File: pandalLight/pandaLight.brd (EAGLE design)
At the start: 100 x 50 mm, 159 parts, among them J1 PJ-037A, U1 MIC23450AAAYML, U12 N25Q128AF8, U13 TPD12S016PWR, U14 AS4C128M16D3, U15 PMOD-2X6, U16 PMOD-2X6, U17 PLR135-T10, U18 PLT133-T10W, U19 PLR135-T10, U2 6SLX45CSG324, U20 TP10SQ, U21 TP10SQ, U22 PAN1322, U23 6SLX9TQG144, U3 TPD4S014SON, U4 FT2232HL, U5 93LC46BT-I/OT, U6 51, U7 51, U8 TPD12S016PWR, X1 USBUB-S, X2 HDMI_RECEPTICAL_A, X4 HDMI_RECEPTICAL_A, Y1 403, Y2 20Mhz

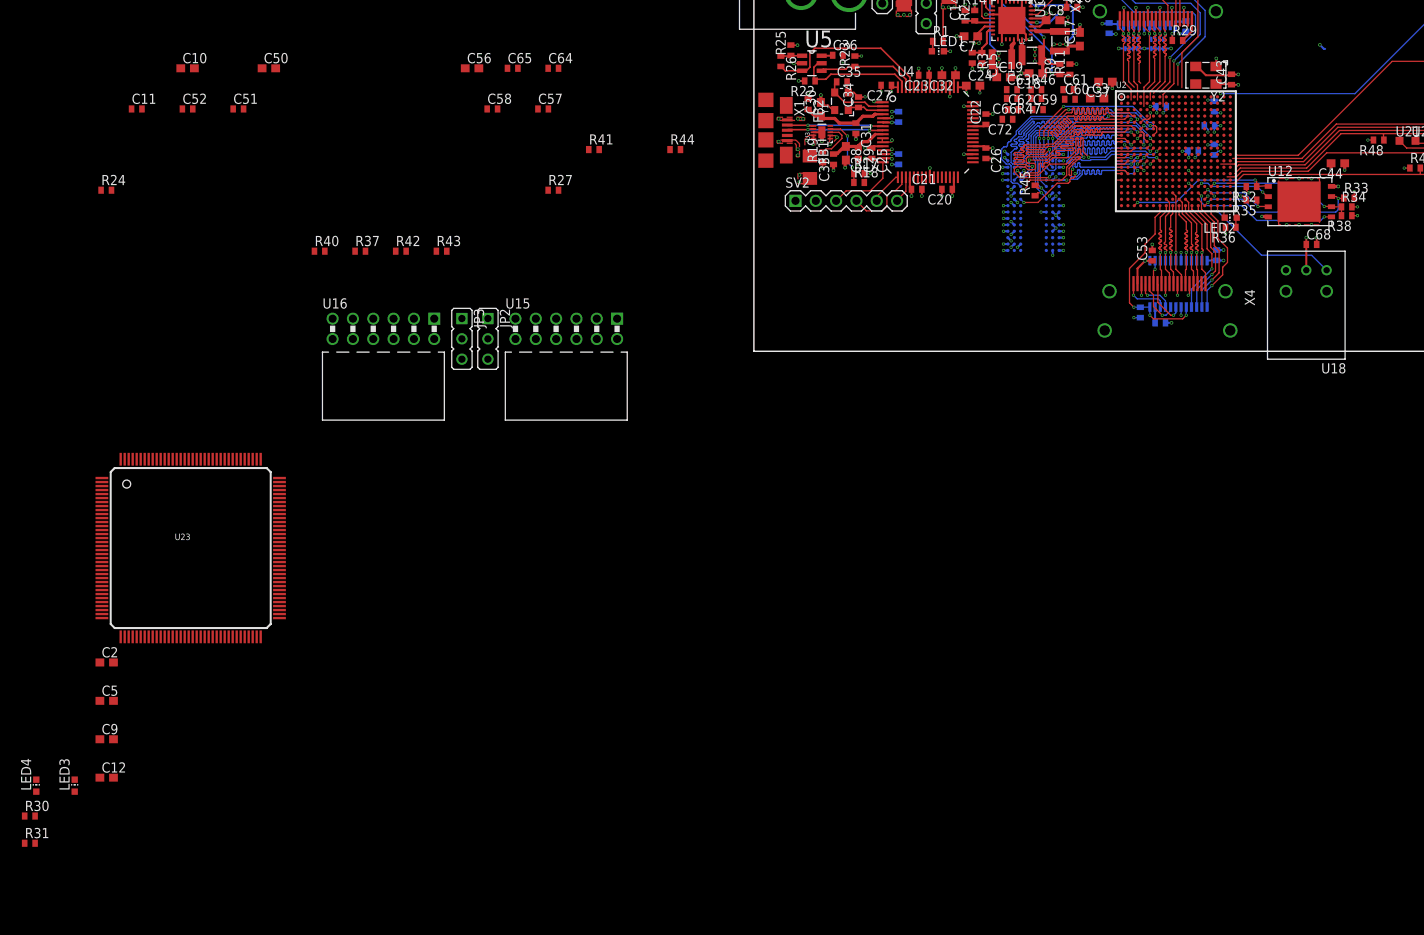
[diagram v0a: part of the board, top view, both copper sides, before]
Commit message: Continued switching to LX9
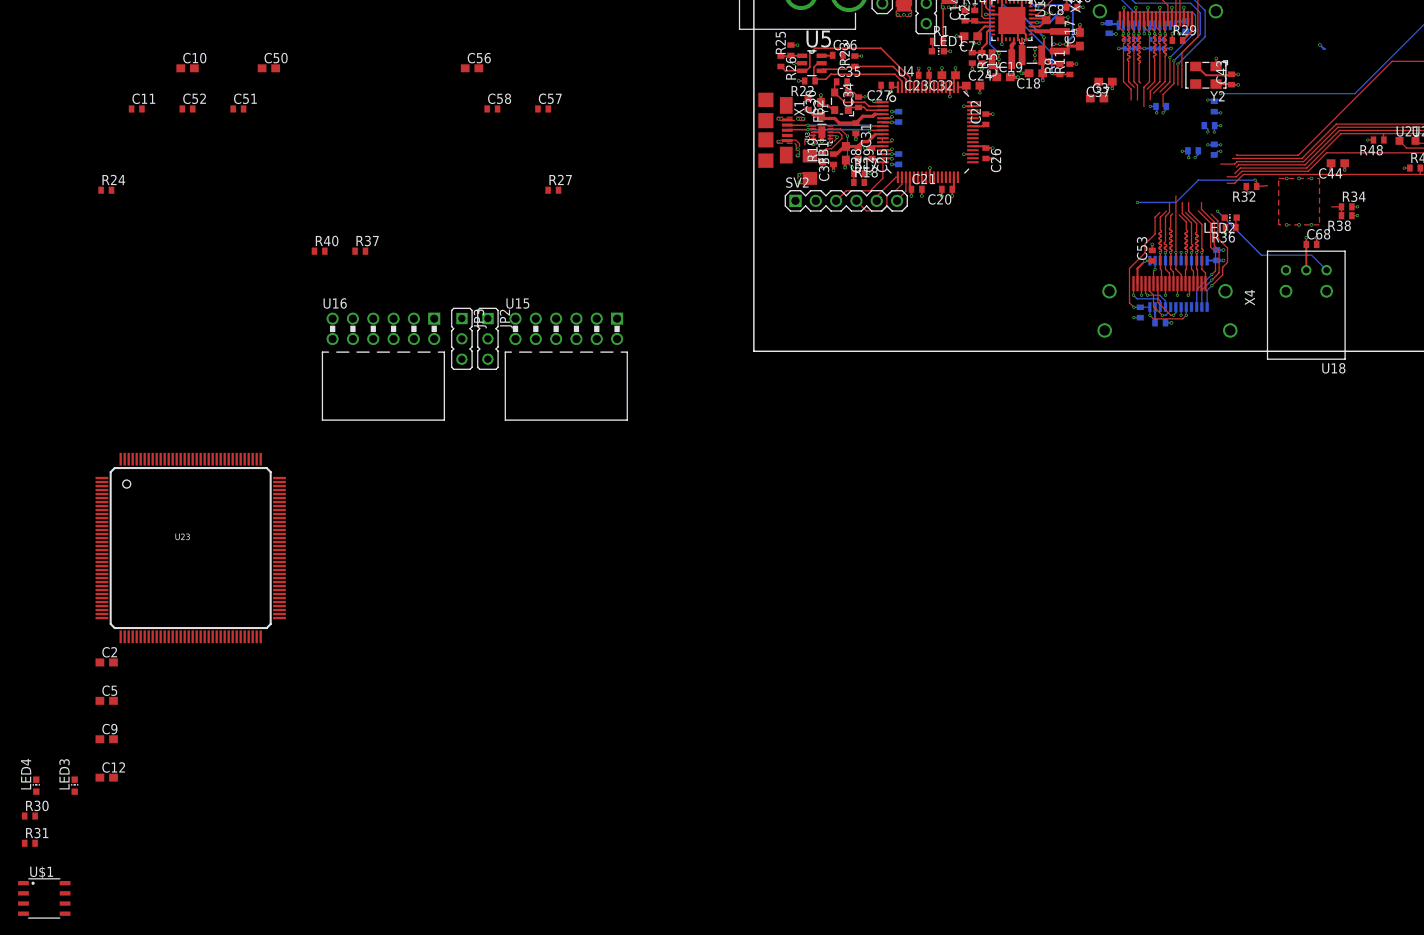
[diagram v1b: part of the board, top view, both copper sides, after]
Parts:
- removed C59, C60: 1u, pandaLight:0402
- removed C61, C62, C63, C64, C65, C66, C72: 0.1u, pandaLight:0402
- removed R33, R35: 10k, pandaLight:0402
- removed R41: 120, pandaLight:0402
- removed R42, R43: 4.7k, pandaLight:0402
- removed R44: 240, pandaLight:0402
- removed R45: 100, pandaLight:0402
- removed R46, R47: 1k, pandaLight:0402
- removed U12: N25Q128AF8, pandaLight:V-PDFN-8_8X6
- removed U14: AS4C128M16D3, pandaLight:96-FBGA_13X9
- removed U2: 6SLX45CSG324, pandaLight:CS324
- added U$1: M25P40-VMN, pandaLight:SO8N
- R30, R31: value 220 -> 1k
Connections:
- removed net +1V5_VREF: C63.2, C64.1, C65.1, C66.1, C72.1, R46.1, R47.2, U14.H1, U14.M8, U2.C1, U2.M5, U2.N3
- removed net DDR3_A0: U14.N3, U2.J7
- removed net DDR3_A1: U14.P7, U2.J6
- removed net DDR3_A10: U14.L7, U2.F4
- removed net DDR3_A11: U14.R7, U2.D3
- removed net DDR3_A12: U14.N7, U2.G6
- removed net DDR3_A2: U14.P3, U2.H5
- removed net DDR3_A3: U14.N2, U2.L7
- removed net DDR3_A4: U14.P8, U2.F3
- removed net DDR3_A5: U14.P2, U2.H4
- removed net DDR3_A6: U14.R8, U2.H3
- removed net DDR3_A7: U14.R2, U2.H6
- removed net DDR3_A8: U14.T8, U2.D2
- removed net DDR3_A9: U14.R3, U2.D1
- removed net DDR3_BA0: U14.M2, U2.F2
- removed net DDR3_BA1: U14.N8, U2.F1
- removed net DDR3_BA2: U14.M3, U2.E1
- removed net DDR3_CAS#: U14.K3, U2.K5
- removed net DDR3_CK: R45.1, U14.J7, U2.G3
- removed net DDR3_CK#: R45.2, U14.K7, U2.G1
- removed net DDR3_CKE: R42.2, U14.K9, U2.H7
- removed net DDR3_DQ0: U14.E3, U2.L2
- removed net DDR3_DQ1: U14.F7, U2.L1
- removed net DDR3_DQ10: U14.C8, U2.N2
- removed net DDR3_DQ11: U14.C2, U2.N1
- removed net DDR3_DQ12: U14.A7, U2.T2
- removed net DDR3_DQ13: U14.A2, U2.T1
- removed net DDR3_DQ14: U14.B8, U2.U2
- removed net DDR3_DQ15: U14.A3, U2.U1
- removed net DDR3_DQ2: U14.F2, U2.K2
- removed net DDR3_DQ3: U14.F8, U2.K1
- removed net DDR3_DQ4: U14.H3, U2.H2
- removed net DDR3_DQ5: U14.H8, U2.H1
- removed net DDR3_DQ6: U14.G2, U2.J3
- removed net DDR3_DQ7: U14.H7, U2.J1
- removed net DDR3_DQ8: U14.D7, U2.M3
- removed net DDR3_DQ9: U14.C3, U2.M1
- removed net DDR3_LDM: U14.E7, U2.K3
- removed net DDR3_LDQS: U14.F3, U2.L4
- removed net DDR3_LDQS#: U14.G3, U2.L3
- removed net DDR3_ODT: U14.K1, U2.K6
- removed net DDR3_RAS#: U14.J3, U2.L5
- removed net DDR3_RESET#: R43.2, U14.T2, U2.E4
- removed net DDR3_UDM: U14.D3, U2.K4
- removed net DDR3_UDQS: U14.C7, U2.P2
- removed net DDR3_UDQS#: U14.B7, U2.P1
- removed net DDR3_WE#: U14.L3, U2.E3
- removed net HDMI_TX0_HPD_3V3: U13.4, U2.V12
- removed net M3_RZQ: R41.1, U2.L6
- removed net N$46: R33.1, U12.7, U2.V14
- removed net N$53: LED4.C, R31.2
- net +1V5: no longer C59.1, C60.1, C61.1, C62.1, C63.1, R46.2, U14.A1, U14.A8, U14.B2, U14.C1, U14.C9, U14.D2, U14.D9, U14.E9, U14.F1, U14.G7, U14.H2, U14.H9, U14.K2, U14.K8, U14.N1, U14.N9, U14.R1, U14.R9, U2.E2, U2.G4, U2.J2, U2.J5, U2.M4, U2.R2
- net +3V3: now also R30.2, R31.2, U$1.3, U$1.7, U$1.8, U23.P103, U23.P122, U23.P125, U23.P135, U23.P42, U23.P63, U23.P69, U23.P76, U23.P86; no longer LED3.A, LED4.A, R33.2, R35.2, U12.8, U2.P9, U2.R12, U2.R6, U2.T15, U2.U14, U2.U4, U2.U9
- net GND: now also U$1.4, U23.P60; no longer C59.2, C60.2, C61.2, C62.2, C64.2, C65.2, C66.2, C72.2, R41.2, R42.1, R43.1, R44.1, R47.1, U12.4, U12.ETP, U14.A9, U14.B1, U14.B3, U14.B9, U14.D1, U14.D8, U14.E1, U14.E2, U14.E8, U14.F9, U14.G1, U14.G8, U14.G9, U14.J2, U14.J8, U14.L2, U14.M1, U14.M9, U14.P1, U14.P9, U14.T1, U14.T9, U2.A1, U2.A18, U2.B13, U2.B7, U2.C16, U2.C3, U2.D10, U2.D5, U2.E15, U2.G12, U2.G17, U2.G2, U2.G5, U2.H10, U2.H8, U2.J11, U2.J15, U2.J4, U2.J9, U2.K10, U2.K8, U2.L11, U2.L9, U2.M17, U2.M2, U2.M6, U2.N12, U2.N13, U2.R1, U2.R14, U2.R18, U2.R4, U2.R9, U2.T16, U2.U12, U2.U6, U2.V1, U2.V18
- net HDMI_TX0_CEC_3V3: no longer U2.V15
- net HDMI_TX0_CLK_N: now also U23.P50; no longer U2.V8
- net HDMI_TX0_CLK_P: now also U23.P51; no longer U2.U8
- net HDMI_TX0_CTRL_EN: no longer U2.V7
- net HDMI_TX0_DATA0_N: now also U23.P55; no longer U2.V9
- net HDMI_TX0_DATA0_P: now also U23.P56; no longer U2.T9
- net HDMI_TX0_DATA1_N: now also U23.P57; no longer U2.V10
- net HDMI_TX0_DATA1_P: now also U23.P58; no longer U2.U10
- net HDMI_TX0_DATA2_N: now also U23.P61; no longer U2.V11
- net HDMI_TX0_DATA2_P: no longer U13.23, U2.U11
- net HDMI_TX0_SCL_3V3: no longer U2.U13
- net HDMI_TX0_SDA_3V3: no longer U2.V13
- net N$3: now also LED4.A, R31.1; no longer R44.2, U14.L8
- net N$33: now also U23.P71; no longer U2.V17
- net N$34: now also U23.P37; no longer U2.V2
- net N$35: now also U23.P144
- net N$37: now also LED3.A, R30.1; no longer LED3.C, R30.2
- net N$39: now also U23.P39; no longer U2.U3
- net N$40: now also U$1.5, U23.P64; no longer U12.5, U2.T13
- net N$41: now also U$1.1, U23.P38; no longer U12.1, U2.V3
- net N$42: now also U$1.6, U23.P70; no longer U12.6, U2.R15
- net N$43: now also U$1.2, U23.P65; no longer U12.2, U2.R13
- net N$44: now also U13.23, U23.P62; no longer R35.1, U12.3, U2.T14
- net TOS_OUT0: no longer U2.V16
- net USB_CTS#: now also U23.P111
- net USB_DCD#: now also U23.P118
- net USB_DSR#: now also U23.P117
- net USB_DTR#: now also U23.P116
- net USB_RI#: now also U23.P119
- net USB_RTS#: now also U23.P112
- net USB_RXD: now also U23.P114
- net USB_RXLED#: now also LED3.C; no longer R30.1
- net USB_TXD: now also U23.P115
- net USB_TXLED#: now also LED4.C; no longer R31.1
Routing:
- net DDR3_WE#: track 26.5 -> 0.00 mm, vias 1 -> 0
- net DDR3_A4: track 26.5 -> 0.00 mm, vias 1 -> 0
- net DDR3_A5: track 26.5 -> 0.00 mm, vias 1 -> 0
- net DDR3_BA1: track 26.5 -> 0.00 mm, vias 1 -> 0
- net DDR3_A11: track 26.5 -> 0.00 mm, vias 1 -> 0
- net DDR3_A2: track 26.5 -> 0.00 mm, vias 1 -> 0
- net DDR3_A0: track 26.5 -> 0.00 mm, vias 3 -> 0
- net DDR3_RAS#: track 26.5 -> 0.00 mm, vias 3 -> 0
- net DDR3_BA0: track 26.5 -> 0.00 mm, vias 1 -> 0
- net DDR3_A1: track 26.5 -> 0.00 mm, vias 1 -> 0
- net DDR3_A9: track 26.5 -> 0.00 mm, vias 1 -> 0
- net DDR3_A7: track 26.5 -> 0.00 mm, vias 1 -> 0
- net DDR3_CAS#: track 26.5 -> 0.00 mm, vias 3 -> 0
- net DDR3_A3: track 26.5 -> 0.00 mm, vias 3 -> 0
- net DDR3_A6: track 26.5 -> 0.00 mm, vias 1 -> 0
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
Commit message: Made new signal connections; Removed old signals; New buck regulator; Reset the board layout
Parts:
- removed C15, C16, C69: 0.1u, pandaLight:0402
- removed C17, C18, C19: 4.7u, pandaLight:0603
- removed L2: 1u, 3A, pandaLight:1008
- removed L5: 47u, pandaLight:0603
- removed R10, R12, R14, R7: 100k, pandaLight:0402
- removed R11: 221k, pandaLight:0402
- removed R13: 274k, pandaLight:0402
- removed R15: 294k, pandaLight:0402
- removed R2, R3, R4: 51, pandaLight:0402
- removed R6: 71.5k, pandaLight:0402
- removed R9: 316k, pandaLight:0402
- removed U1: MIC23450AAAYML, pandaLight:QFN-32-5X5
- removed U19: PLR135-T10, pandaLight:PLR135-T10_PLT133-T10W
- added C13: 10u, pandaLight:0603
- added SV3: (no value), pandaLight:MA02-1
- added U$2: MIC2230-XXYML, pandaLight:MLF-12
- C14: value 0.1u -> 10u; device pandaLight:0402 -> pandaLight:0603
- L1, L3: value 1u, 3A -> 2.2u, 1.3A
- R5: value 309k -> 100k
- moved U20 208.2 mm to (-102.9, 120.7)
- moved C68 198.7 mm to (-102.9, 111.8)
- moved C67 197.0 mm to (-97.8, 111.8), turned to 0 degrees
- moved R49 192.6 mm to (-82.5, 121.9)
- moved L4 190.1 mm to (-87.6, 121.9), turned to 0 degrees
- moved R31 187.4 mm to (-52.1, 121.9)
- moved R30 185.2 mm to (-47.0, 121.9)
- moved R48 182.6 mm to (-77.5, 121.9), turned to 0 degrees
- moved C44 180.9 mm to (-87.6, 106.7), turned to 0 degrees
- moved C55 180.6 mm to (-92.7, 111.8), flipped to the top, turned to 0 degrees
- moved R38 176.1 mm to (-67.3, 121.9), turned to 0 degrees
- moved C54 175.7 mm to (-87.6, 111.8), flipped to the top, turned to 0 degrees
- moved R39 168.1 mm to (-72.4, 121.9), flipped to the top, turned to 0 degrees
- moved R34 167.4 mm to (-57.1, 121.9)
- moved C53 165.8 mm to (-82.5, 111.8), turned to 0 degrees
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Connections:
- removed net FPGA_OSC1: Y2.3
- removed net N$14: L1.1, U1.26
- removed net N$15: C16.1, R4.1, U1.28
- removed net N$16: L2.1, U1.23
- removed net N$17: L3.1, U1.21
- removed net N$18: R13.1, R15.1, U1.10
- removed net N$20: R10.2, U1.6
- removed net N$21: R5.1, R6.1, U1.32
- removed net N$22: R7.2, U1.1
- removed net N$23: R11.1, R9.1, U1.5
- removed net N$24: R12.2, U1.3
- removed net N$26: R14.2, U1.12
- removed net N$30: C15.1, R3.1, U1.15
- removed net N$48: C14.1, R2.1, U1.13
- removed net TOS_IN1: U19.3
- new net FPGA_CLK20: U23.P21, Y2.3
- new net LEDS_CLK: SV3.2, U23.P5
- new net LEDS_DATA: SV3.1, U23.P6
- new net SW1: L1.1, U$2.8
- new net SW2: L3.1, U$2.4
- net +1V2: now also C14.1, U$2.1; no longer C19.1, R13.2, R14.1, U1.9
- net +1V5: now also U23.P18, U23.P31, U23.P4; no longer C18.1, L2.2, R10.1, R9.2, U1.4
- net +3V3: now also C13.1, U$2.12; no longer C17.1, L5.1, R5.2, R7.1, U1.31
- net +5V: now also R5.1, U$2.3, U$2.9; no longer R12.1, R2.2, R3.2, R4.2, U1.14, U1.27, U1.29
- net GND: now also C13.2, U$2.5, U$2.6; no longer C15.2, C16.2, C17.2, C18.2, C19.2, C69.2, R11.2, R15.2, R6.2, U1.11, U1.18, U1.2, U1.22, U1.24, U1.7, U1.ETP, U19.2
- net HDMI_TX0_CEC_3V3: now also U23.P48
- net HDMI_TX0_CTRL_EN: now also U23.P45
- net HDMI_TX0_SCL_3V3: now also U23.P47
- net HDMI_TX0_SDA_3V3: now also U23.P46
- net N$25: now also U$2.11; no longer U1.30
- net N$27: now also U$2.2; no longer U1.8
- net N$4: now also R5.2, U$2.7; no longer C69.1, L5.2, U19.1
- net TOS_IN0: now also U23.P124
- net TOS_OUT0: now also U23.P44
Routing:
- net GND: track 120.7 -> 0.00 mm, vias 115 -> 0
- net +3V3: track 77.0 -> 0.00 mm, vias 49 -> 0
- net TOS_IN0: track 37.6 -> 0.00 mm, vias 1 -> 0
- net BT_TX: track 36.7 -> 0.00 mm
- net BT_RTS: track 36.5 -> 0.00 mm
- net TOS_IN1: track 34.5 -> 0.00 mm
- net BT_RX: track 33.7 -> 0.00 mm
- net BT_CTS: track 32.2 -> 0.00 mm
- net BT_WAKE: track 32.1 -> 0.00 mm
- net BT_RESET#: track 30.5 -> 0.00 mm
- net HDMI_RX0_SCL_3V3: track 25.9 -> 0.00 mm, vias 1 -> 0
- net HDMI_RX0_CEC_3V3: track 24.2 -> 0.00 mm, vias 1 -> 0
- net HDMI_RX0_CTRL_EN: track 23.0 -> 0.00 mm, vias 3 -> 0
- net HDMI_RX0_SDA_3V3: track 22.9 -> 0.00 mm, vias 1 -> 0
- net HDMI_TX0_CTRL_EN: track 22.6 -> 0.00 mm, vias 3 -> 0
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- removed copper zone on layer 1, net +1V2
- removed copper zone on layer 1, net +1V5
- removed copper zone on layer 16, net +1V5
- removed copper zone on layer 15, net +1V8
- removed copper zone on layer 1, net +3V3
- removed copper zone on layer 15, net +3V3
- removed copper zone on layer 16, net +3V3
- removed copper zone on layer 1, net +5V
- removed copper zone on layer 15, net +5V
- removed copper zone on layer 1, net CENTER
- removed copper zone on layer 1, net GND
- removed copper zone on layer 2, net GND
- removed copper zone on layer 15, net N$32
- removed copper zone on layer 1, net N$45
- removed copper zone on layer 15, net N$45
- removed copper zone on layer 2, net N$52
- removed copper zone on layer 1, net USB_VBUS
- removed copper zone on layer 15, net USB_VBUS
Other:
- board size 100 x 50 mm -> 160 x 100 mm

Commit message: Created BOM; Began routing; Changed to available LEDs
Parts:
- removed C1: 100u, pandaLight:1206
- removed LED3: Green, pandaLight:LED-0603
- removed LED4: Yellow, pandaLight:LED-0603
- removed R30, R31: 1k, pandaLight:0402
- SV3: value (none) -> LEDS_CON; device pandaLight:MA02-1 -> pandaLight:MA04-1
- moved C20 164.7 mm to (61.0, 90.0)
- moved C30 143.9 mm to (70.0, 85.8)
- moved C28 139.2 mm to (70.0, 83.8)
- moved R8 134.5 mm to (34.6, 86.2), turned to 270 degrees
- moved U4 133.0 mm to (65.6, 71.2)
- moved SV3 131.4 mm to (31.6, 91.3)
- moved R5 126.7 mm to (32.2, 80.6), turned to 90 degrees
- moved C31 126.2 mm to (70.0, 79.8)
- moved R1 122.1 mm to (24.4, 83.2)
- moved C29 121.0 mm to (70.0, 80.8)
- moved FB2 119.0 mm to (62.4, 84.2)
- moved FB1 114.6 mm to (62.4, 82.6)
- moved C13 100.1 mm to (35.4, 78.6)
- moved C14 98.9 mm to (29.0, 78.6), turned to 180 degrees
- moved SV1 98.7 mm to (17.4, 90.0), turned to 270 degrees
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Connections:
- net HDMI_RX0_5V renamed HDMI_RX_5V
- net HDMI_RX0_CEC renamed HDMI_RX_CEC
- net HDMI_RX0_CEC_3V3 renamed HDMI_RX_CEC_3V3
- net HDMI_RX0_CLK_N renamed HDMI_RX_CLK_N
- net HDMI_RX0_CLK_P renamed HDMI_RX_CLK_P
- net HDMI_RX0_CTRL_EN renamed HDMI_RX_CTRL_EN
- net HDMI_RX0_DATA0_N renamed HDMI_RX_DATA0_N
- net HDMI_RX0_DATA0_P renamed HDMI_RX_DATA0_P
- net HDMI_RX0_DATA1_N renamed HDMI_RX_DATA1_N
- net HDMI_RX0_DATA1_P renamed HDMI_RX_DATA1_P
- net HDMI_RX0_DATA2_N renamed HDMI_RX_DATA2_N
- net HDMI_RX0_DATA2_P renamed HDMI_RX_DATA2_P
- net HDMI_RX0_SCL_3V3 renamed HDMI_RX_SCL_3V3
- net HDMI_RX0_SCL_5V renamed HDMI_RX_SCL_5V
- net HDMI_RX0_SDA_3V3 renamed HDMI_RX_SDA_3V3
- net HDMI_RX0_SDA_5V renamed HDMI_RX_SDA_5V
- net HDMI_TX0_5V renamed HDMI_TX_5V
- net HDMI_TX0_CEC renamed HDMI_TX_CEC
- net HDMI_TX0_CEC_3V3 renamed HDMI_TX_CEC_3V3
- net HDMI_TX0_CLK_N renamed HDMI_TX_CLK_N
- net HDMI_TX0_CLK_P renamed HDMI_TX_CLK_P
- net HDMI_TX0_CTRL_EN renamed HDMI_TX_CTRL_EN
- net HDMI_TX0_DATA0_N renamed HDMI_TX_DATA0_N
- net HDMI_TX0_DATA0_P renamed HDMI_TX_DATA0_P
- net HDMI_TX0_DATA1_N renamed HDMI_TX_DATA1_N
- net HDMI_TX0_DATA1_P renamed HDMI_TX_DATA1_P
- net HDMI_TX0_DATA2_N renamed HDMI_TX_DATA2_N
- net HDMI_TX0_HPD_5V renamed HDMI_TX_HPD_5V
- net HDMI_TX0_SCL_3V3 renamed HDMI_TX_SCL_3V3
- net HDMI_TX0_SCL_5V renamed HDMI_TX_SCL_5V
- net HDMI_TX0_SDA_3V3 renamed HDMI_TX_SDA_3V3
- net HDMI_TX0_SDA_5V renamed HDMI_TX_SDA_5V
- net TOS_IN0 renamed TOS_IN
- net TOS_OUT0 renamed TOS_OUT
- removed net CENTER: C6.1, J1.CENTER, JP1.1, SV1.1
- removed net HDMI_TX0_DATA2_P: X4.1
- removed net N$3: LED4.A, R31.1
- removed net N$37: LED3.A, R30.1
- removed net N$44: U13.23, U23.P62
- removed net USB_RXLED#: LED3.C, U4.54
- removed net USB_TXLED#: LED4.C, U4.55
- new net 5V_SUP: C6.1, J1.CENTER, JP1.1, SV1.1, SV3.1
- new net HDMI_TX_DATA2_P: U13.23, U23.P62, X4.1
- net +3V3: no longer R30.2, R31.2
- net +5V: no longer C1.1
- net GND: now also SV3.4, U$2.EP; no longer C1.2
- net LEDS_CLK: now also SV3.3; no longer SV3.2
- net LEDS_DATA: now also SV3.2; no longer SV3.1
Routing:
- net +5V: track 0.00 -> 34.5 mm
- net +1V2: track 0.00 -> 13.6 mm, vias 0 -> 2
- net 5V_SUP: track 0.00 -> 5.93 mm
- net GND: track 0.00 -> 5.36 mm, vias 0 -> 11
- net SW2: track 0.00 -> 3.48 mm
- net N$4: track 0.00 -> 3.16 mm
- net SW1: track 0.00 -> 2.92 mm
- net N$47: track 0.00 -> 1.44 mm
- net N$27: track 0.00 -> 1.12 mm
- net N$25: track 0.00 -> 1.12 mm
- added copper zone on layer 1, net +3V3
- added copper zone on layer 1, net 5V_SUP
- added copper zone on layer 1, net GND
- added copper zone on layer 16, net GND

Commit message: Little bit of routing
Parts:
- moved R22 124.5 mm to (16.6, 81.8)
- moved X1 89.1 mm to (1.50, 71.4), turned to 270 degrees
- moved C24 89.1 mm to (22.2, 78.2), turned to 90 degrees
- moved C27 84.4 mm to (27.0, 63.0)
- moved C36 79.2 mm to (16.6, 83.0)
- moved C26 78.6 mm to (24.0, 62.0)
- moved C25 75.7 mm to (24.0, 60.6)
- moved C28 56.4 mm to (22.2, 53.8)
- moved C22 56.4 mm to (19.0, 60.4)
- moved C21 56.3 mm to (13.2, 59.2)
- moved C23 56.3 mm to (18.2, 59.2)
- moved C30 56.3 mm to (22.2, 56.0)
- moved C31 56.3 mm to (22.2, 50.0)
- moved FB1 56.3 mm to (14.6, 52.8)
- moved FB2 56.3 mm to (14.6, 54.4)
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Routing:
- net +1V8: track 0.00 -> 27.1 mm
- net GND: track 5.36 -> 21.5 mm, vias 11 -> 22
- net N$10: track 0.00 -> 10.2 mm, vias 0 -> 2
- net N$6: track 0.00 -> 7.77 mm
- net N$8: track 0.00 -> 7.72 mm
- net N$7: track 0.00 -> 7.70 mm
- net N$9: track 0.00 -> 5.59 mm
- net N$12: track 0.00 -> 3.62 mm
